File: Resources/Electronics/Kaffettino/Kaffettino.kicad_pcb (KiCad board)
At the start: 2 copper layers, 150 x 150 mm, 64 parts, among them J2 OSTVN02A150, J3 OSTVN04A150, J4 OSTVN04A150, J5 OSTVN04A150, M1 RFID-RC522, Q1 PN2222A, U1 PCF8574AN, U2 DFR0299, U3 ESP32-38Pin-Wroom, U4 26052

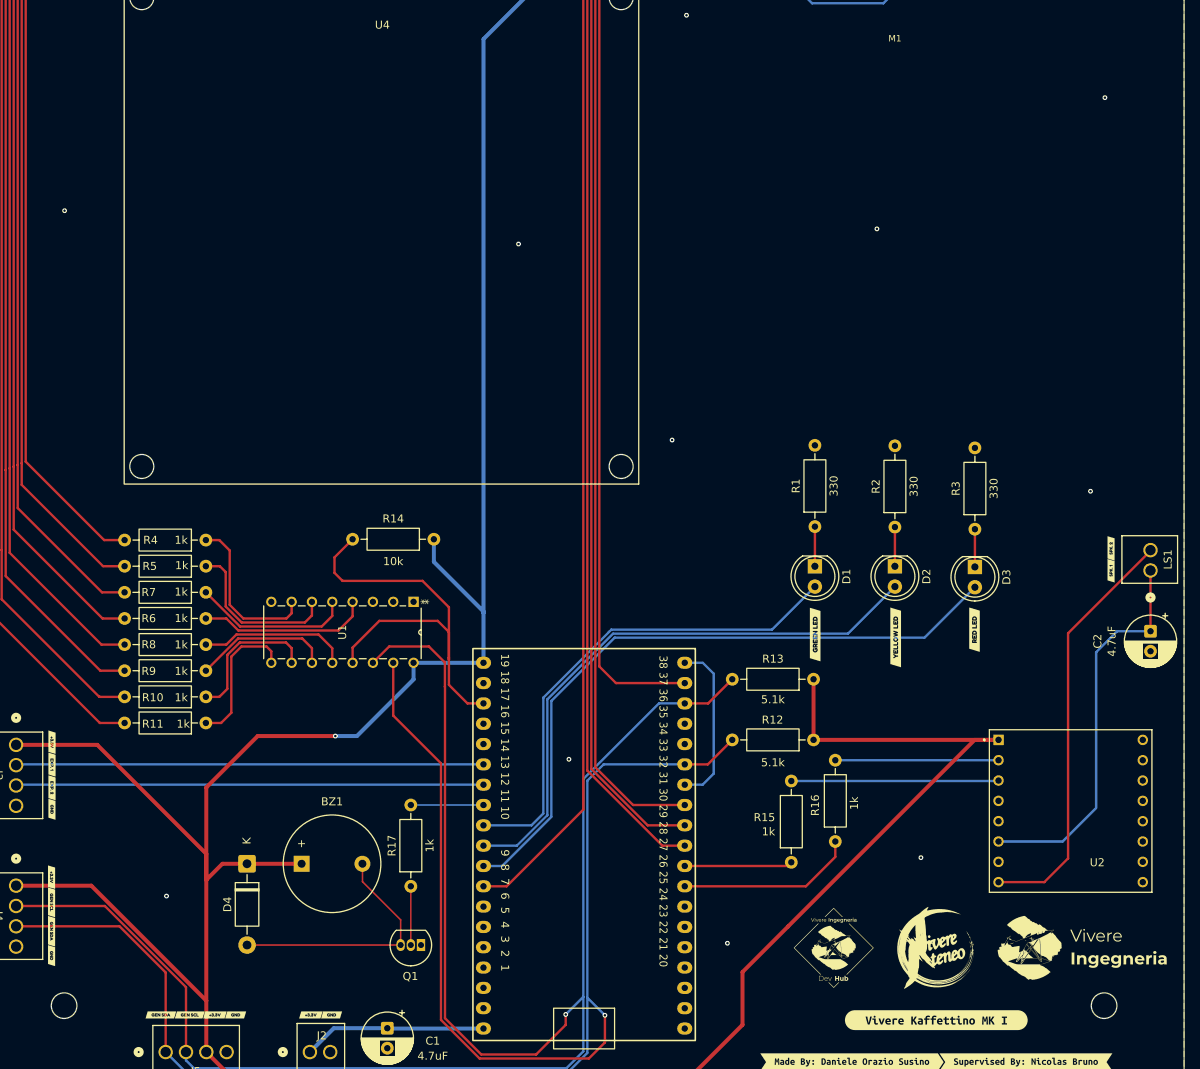
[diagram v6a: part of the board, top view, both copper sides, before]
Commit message: Embedded: Incresed size of silkscreen
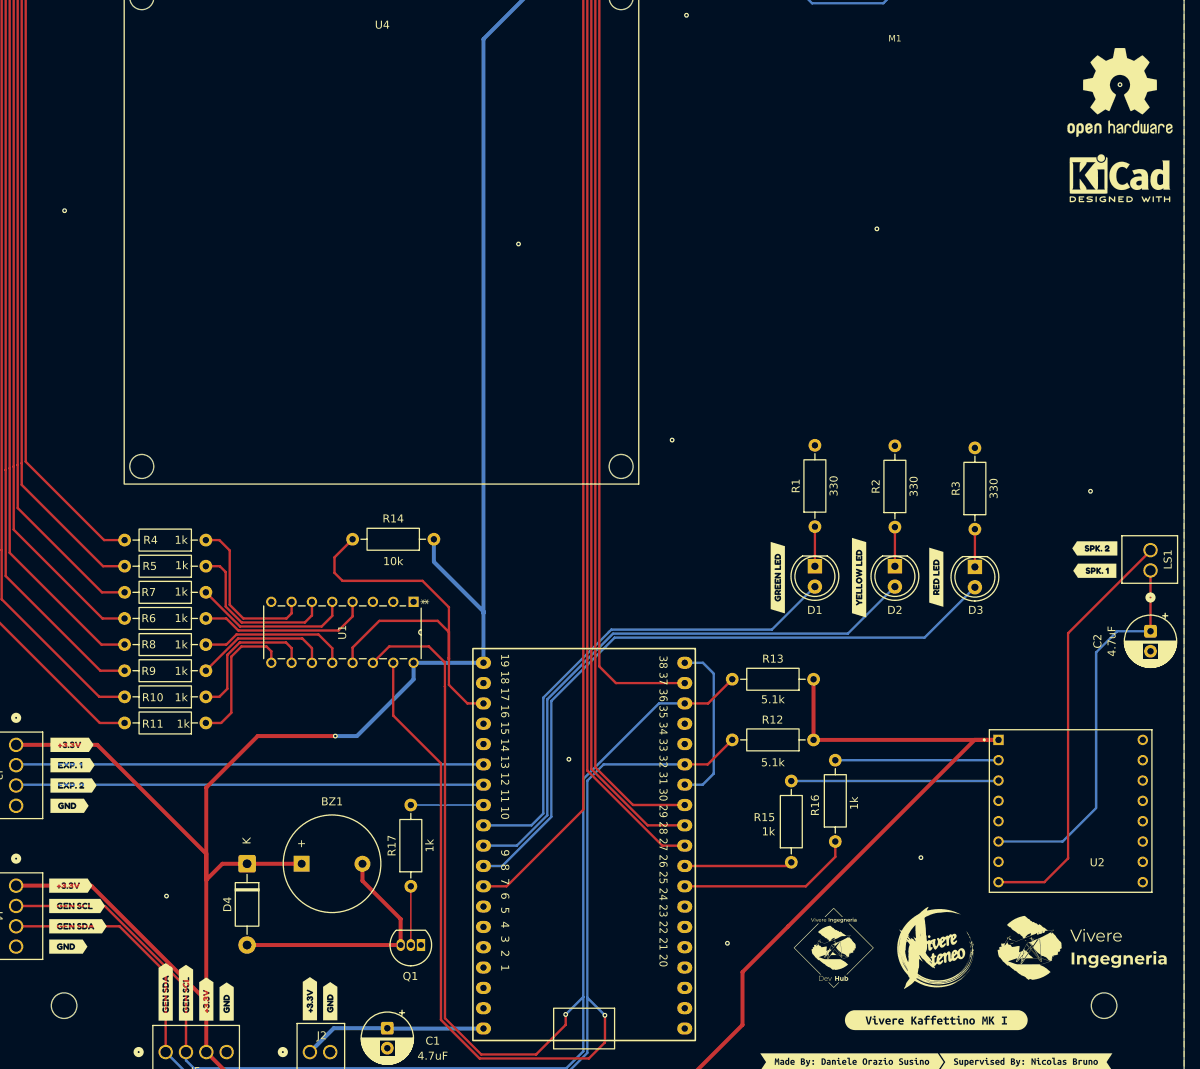
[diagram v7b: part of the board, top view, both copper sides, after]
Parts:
- removed kibuzzard-69A0D4B7 (x4): G***, kibuzzard-69A0D4B7
- removed kibuzzard-69A0D4BD (x4): G***, kibuzzard-69A0D4BD
- removed kibuzzard-69A0D4C4 (x2): G***, kibuzzard-69A0D4C4
- removed kibuzzard-69A0D4CC (x2): G***, kibuzzard-69A0D4CC
- removed kibuzzard-69A0D614: G***, kibuzzard-69A0D614
- removed kibuzzard-69A0D627: G***, kibuzzard-69A0D627
- removed kibuzzard-69A0D881: G***, kibuzzard-69A0D881
- removed kibuzzard-69A0D88A: G***, kibuzzard-69A0D88A
- removed kibuzzard-69A0DE3E: G***, kibuzzard-69A0DE3E
- removed kibuzzard-69A0DE44: G***, kibuzzard-69A0DE44
- removed kibuzzard-69A0DE4A: G***, kibuzzard-69A0DE4A
- added REF**: OSHW-Logo2_14.6x12mm_SilkScreen, Symbol:OSHW-Logo2_14.6x12mm_SilkScreen, F.Cu at (162.0, 40.8)
- added REF**: KiCad-Logo2_5mm_SilkScreen, Symbol:KiCad-Logo2_5mm_SilkScreen, F.Cu at (162.0, 51.6)
- added kibuzzard-69A1A68F: G***, kibuzzard-69A1A68F, F.Cu at (139.0, 101.4)
- added kibuzzard-69A1A695: G***, kibuzzard-69A1A695, F.Cu at (129.4, 101.5)
- added kibuzzard-69A1A69C: G***, kibuzzard-69A1A69C, F.Cu at (119.2, 101.5)
- added kibuzzard-69A1A9EC: G***, kibuzzard-69A1A9EC, F.Cu at (31.1, 124.9)
- added kibuzzard-69A1A9F8: G***, kibuzzard-69A1A9F8, F.Cu at (31.0, 122.4)
- added kibuzzard-69A1AA1D: G***, kibuzzard-69A1AA1D, F.Cu at (31.2, 127.5)
- added kibuzzard-69A1AA21: G***, kibuzzard-69A1AA21, F.Cu at (30.7, 130.0)
- added kibuzzard-69A1AA26: G***, kibuzzard-69A1AA26, F.Cu at (30.8, 140.0)
- added kibuzzard-69A1AA29: G***, kibuzzard-69A1AA29, F.Cu at (31.6, 142.5)
- added kibuzzard-69A1AA2F: G***, kibuzzard-69A1AA2F, F.Cu at (31.7, 145.1)
- added kibuzzard-69A1AA32: G***, kibuzzard-69A1AA32, F.Cu at (30.5, 147.6)
- added kibuzzard-69A1AB0D: G***, kibuzzard-69A1AB0D, F.Cu at (42.7, 153.3)
- added kibuzzard-69A1AB14: G***, kibuzzard-69A1AB14, F.Cu at (45.2, 153.4)
- added kibuzzard-69A1AB1B: G***, kibuzzard-69A1AB1B, F.Cu at (47.8, 154.2)
- added kibuzzard-69A1AB21: G***, kibuzzard-69A1AB21, F.Cu at (50.3, 154.5)
- added kibuzzard-69A1ABE5: G***, kibuzzard-69A1ABE5, F.Cu at (60.7, 154.1)
- added kibuzzard-69A1ABEC: G***, kibuzzard-69A1ABEC, F.Cu at (63.3, 154.4)
- added kibuzzard-69A1AC24: G***, kibuzzard-69A1AC24, F.Cu at (158.8, 97.8)
- added kibuzzard-69A1AC2A: G***, kibuzzard-69A1AC2A, F.Cu at (158.8, 100.6)

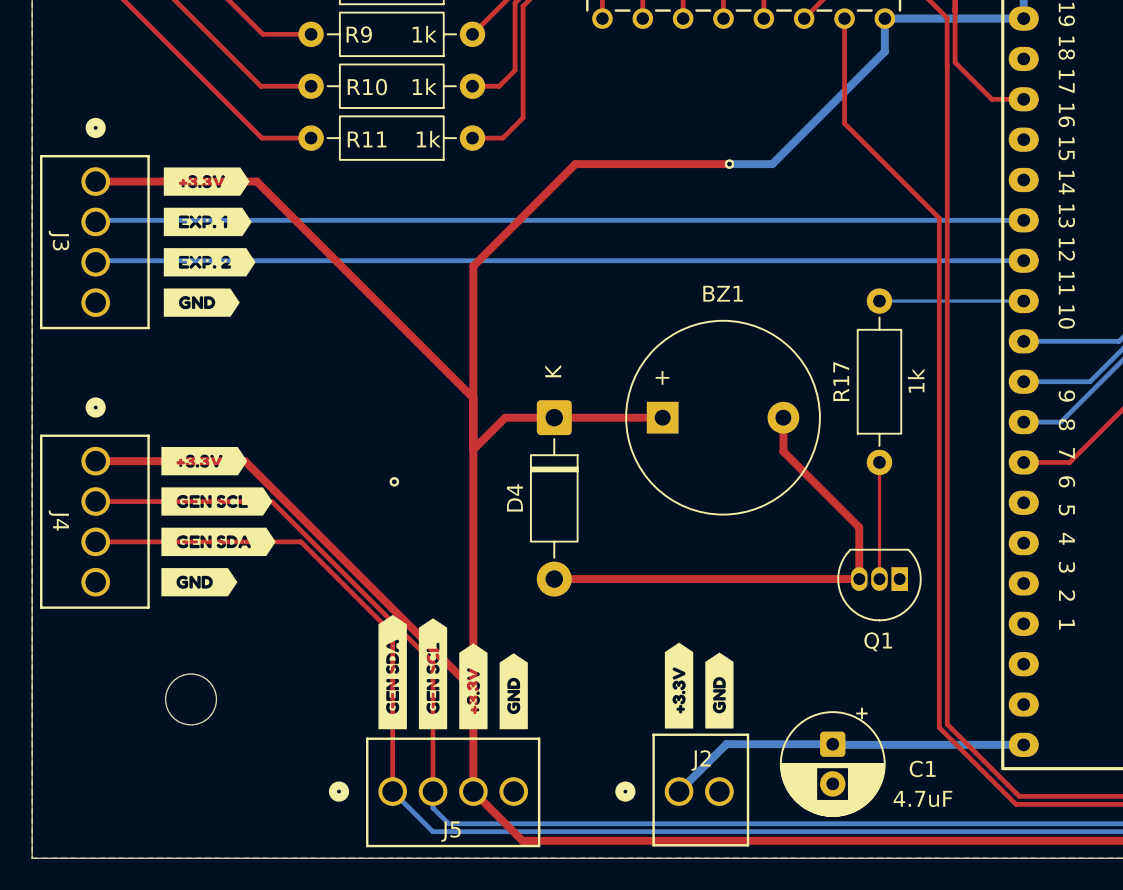
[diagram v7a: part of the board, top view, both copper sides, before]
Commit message: Embedded: Added 5V to expansion headers
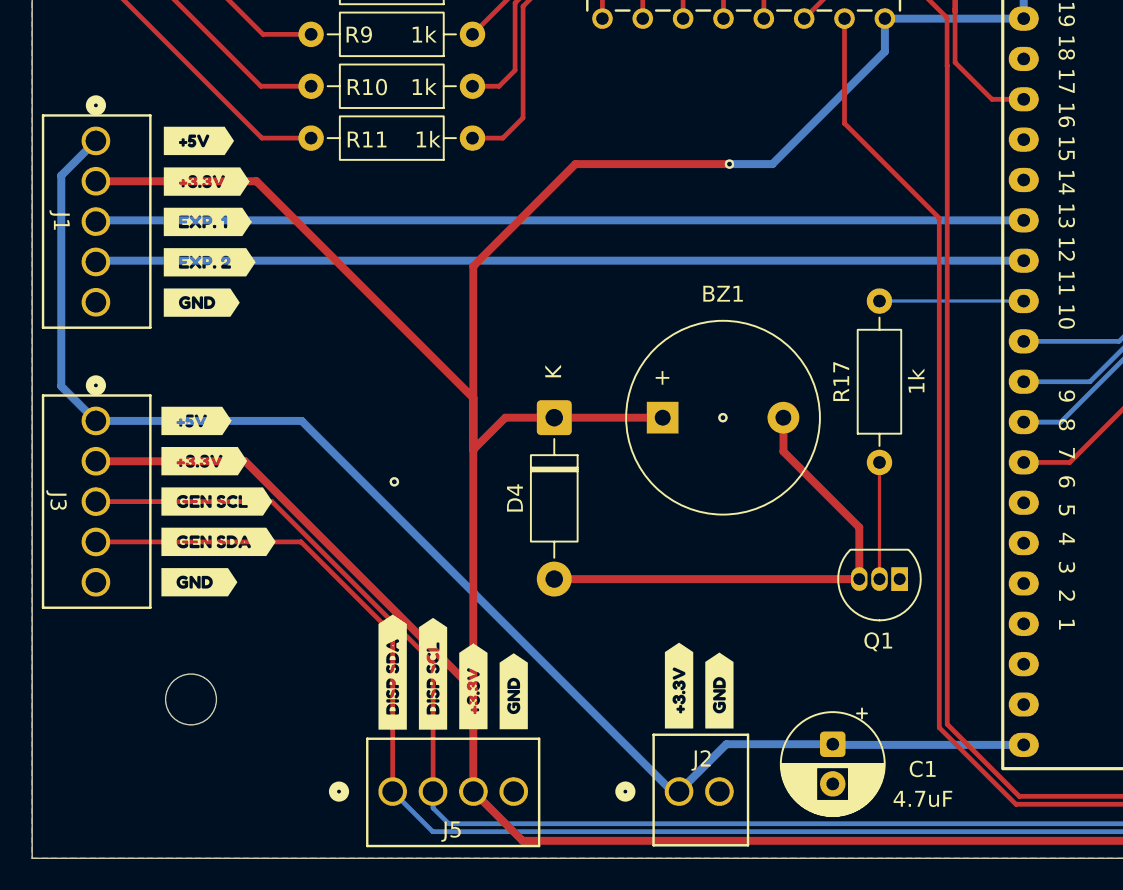
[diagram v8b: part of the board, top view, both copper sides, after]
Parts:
- removed J4: OSTVN04A150, OSTVN04A150:CONN_OSTVN04A150_OST
- removed kibuzzard-69A1AB0D: G***, kibuzzard-69A1AB0D
- removed kibuzzard-69A1AB14: G***, kibuzzard-69A1AB14
- added J1: OSTVN05A150, OSTVN05A150:CONN5_516x256_OST, F.Cu at (24.0, 119.8)
- added kibuzzard-69A1B1F4: G***, kibuzzard-69A1B1F4, F.Cu at (42.7, 153.3)
- added kibuzzard-69A1B1FA: G***, kibuzzard-69A1B1FA, F.Cu at (45.2, 153.4)
- added kibuzzard-69A1B2CD: G***, kibuzzard-69A1B2CD, F.Cu at (30.5, 119.8)
- added kibuzzard-69A1B2CD: G***, kibuzzard-69A1B2CD, F.Cu at (30.3, 137.5)
- J3: value OSTVN04A150 -> OSTVN05A150; footprint OSTVN04A150:CONN_OSTVN04A150_OST -> OSTVN05A150:CONN5_516x256_OST
- moved J3 15.1 mm to (24.0, 137.5), turned to 90 degrees
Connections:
- J3 pad 1: +3.3V -> +5V
- J3 pad 2: /EXPANSION_1 -> +3.3V
- J3 pad 3: /EXPANSION_2 -> /GEN_SCL
- J3 pad 4: GNDREF -> /GEN_SDA
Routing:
- net +5V: track 23.0 -> 88.8 mm
- net GNDREF: vias 11 -> 12
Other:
- board text added: "AI - Actually Indians API - A Person in India LLM - Low-cost Labour in Mumbai AGI - A Genius Indian GPT - Gujarati Professional Typist"
- board text removed: "AI - Actually Indians API - A Person in India LLM - Low-cost Labour in Mumbai AGI - A Genius Indian GPT - Gujjarati Professional Typist"
